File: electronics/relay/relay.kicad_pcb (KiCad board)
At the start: 2 copper layers, 17 x 49 mm, 16 parts, among them J1 Conn_01x01_Female, J2 Conn_01x01_Female, J3 Conn_01x01_Female, J4 Conn_01x01_Female, J5 Conn_01x01_Female, J6 Conn_01x01_Female, J7 Conn_01x01_Female, J8 Conn_01x01_Female, J9 Conn_01x01_Female, K1 SANYOU_SRD_Form_C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

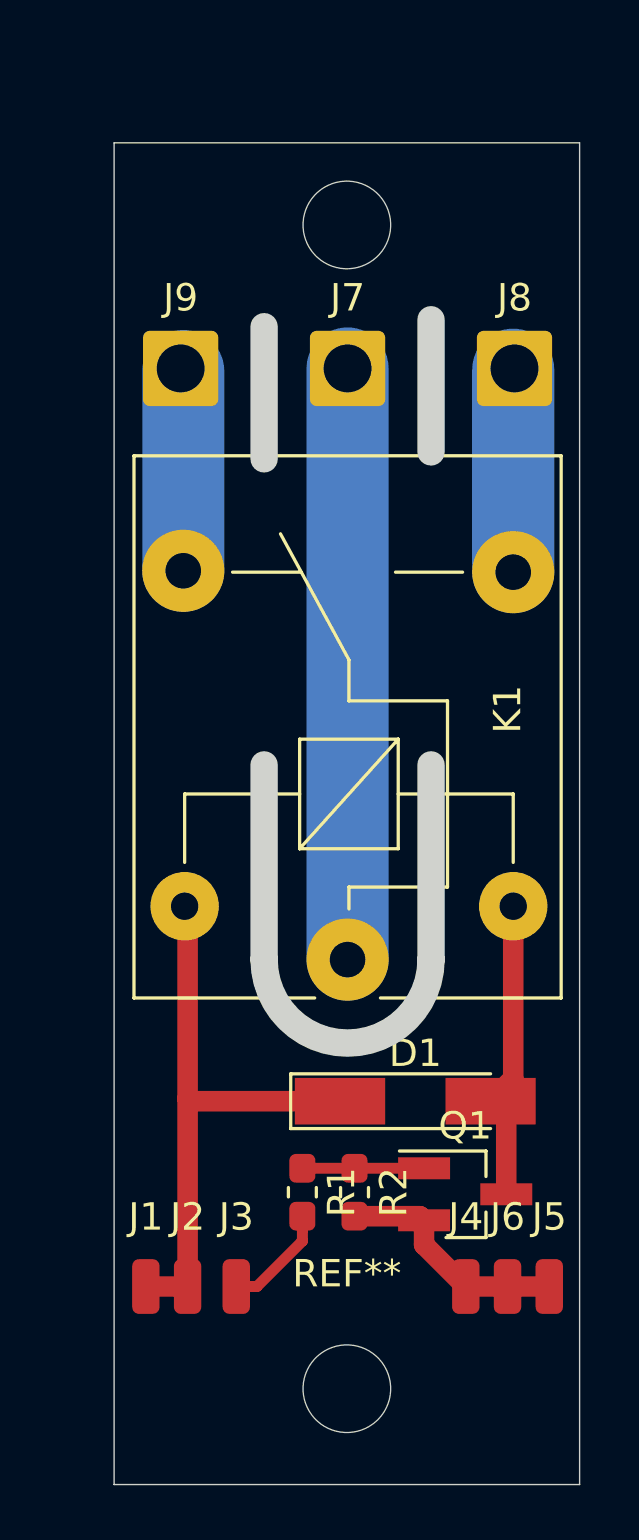
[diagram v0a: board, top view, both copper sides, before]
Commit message: Relay board ready, ESP3266 redesign (GPIO16 instead of GPIO0)
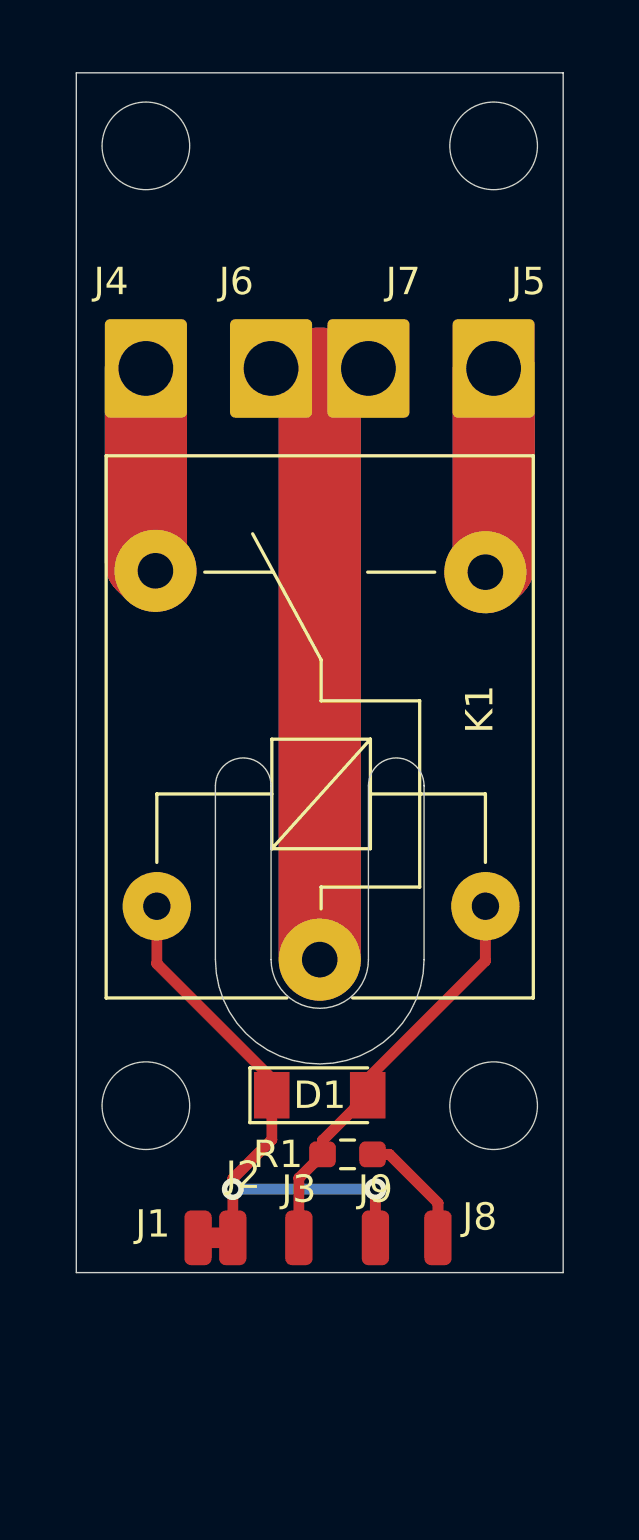
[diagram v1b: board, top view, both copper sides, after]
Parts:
- removed Q1: Q_NMOS_GSD, Package_TO_SOT_SMD:SOT-23_Handsoldering
- removed R2: R_Small, Resistor_SMD:R_0603_1608Metric_Pad1.05x0.95mm_HandSolder
- removed the REF** at (144.5, 116.0)
- removed the REF** at (144.5, 73.5)
- added REF**: MountingHole_3.2mm_M3, MountingHole:MountingHole_3.2mm_M3, F.Cu at (149.9, 70.6)
- added REF**: MountingHole_3.2mm_M3, MountingHole:MountingHole_3.2mm_M3, F.Cu at (149.9, 105.7)
- added REF**: MountingHole_3.2mm_M3, MountingHole:MountingHole_3.2mm_M3, F.Cu at (137.2, 70.6)
- added REF**: MountingHole_3.2mm_M3, MountingHole:MountingHole_3.2mm_M3, F.Cu at (137.2, 105.7)
- D1: footprint Diode_SMD:D_MiniMELF_Handsoldering -> Diode_SMD:D_MiniMELF
- J4, J5, J6: footprint Connector_Wire:SolderWirePad_1x01_SMD_1x2mm -> Powerstrip:SolderWire-Mains
- J7: footprint Connector_Wire:SolderWire-1sqmm_1x01_D1.4mm_OD2.7mm -> Powerstrip:SolderWire-Mains
- J8, J9: footprint Connector_Wire:SolderWire-1sqmm_1x01_D1.4mm_OD2.7mm -> Connector_Wire:SolderWirePad_1x01_SMD_1x2mm
- R1: value R_Small -> 470R; footprint Resistor_SMD:R_0603_1608Metric_Pad1.05x0.95mm_HandSolder -> Resistor_SMD:R_0603_1608Metric_Pad0.98x0.95mm_HandSolder
- moved J4 35.5 mm to (137.2, 78.7), turned to 180 degrees
- moved J6 34.6 mm to (141.7, 78.7), turned to 180 degrees
- moved J5 33.6 mm to (149.9, 78.7), turned to 180 degrees
- moved J9 32.5 mm to (145.5, 110.5)
- moved J8 31.9 mm to (147.8, 110.5)
- moved D1 3.50 mm to (143.5, 105.3)
- moved J3 2.90 mm to (142.7, 110.5)
- moved J1 2.61 mm to (139.1, 110.5)
- moved J2 2.43 mm to (140.3, 110.5)
- moved R1 2.15 mm to (144.5, 107.4), turned to 180 degrees
- moved K1 1.02 mm to (143.5, 100.3)
- moved J7 0.76 mm to (145.3, 78.7), turned to 180 degrees
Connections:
- J3 pad 1: Net-(J3-Pad1) -> Net-(D1-Pad2)
- J4 pad 1: GND -> Net-(J4-Pad1)
- J5 pad 1: GND -> Net-(J5-Pad1)
- J6 pad 1: GND -> Net-(J6-Pad1)
- J7 pad 1: Net-(J7-Pad1) -> Net-(J6-Pad1)
- J9 pad 1: Net-(J9-Pad1) -> Net-(D1-Pad1)
- K1 pad 1: Net-(J7-Pad1) -> Net-(J6-Pad1)
- K1 pad 3: Net-(J8-Pad1) -> Net-(J5-Pad1)
- K1 pad 4: Net-(J9-Pad1) -> Net-(J4-Pad1)
- R1 pad 1: Net-(Q1-Pad1) -> Net-(J8-Pad1)
- R1 pad 2: Net-(J3-Pad1) -> Net-(D1-Pad2)
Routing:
- net Net-(J6-Pad1): track 0.00 -> 46.7 mm
- net Net-(J7-Pad1): track 21.6 -> 0.00 mm
- net Net-(J5-Pad1): track 0.00 -> 15.1 mm
- net Net-(J4-Pad1): track 0.00 -> 15.1 mm
- net GND: track 8.70 -> 0.00 mm
- net Net-(J9-Pad1): track 7.43 -> 0.00 mm
- net Net-(Q1-Pad1): track 4.44 -> 0.00 mm
- net Net-(J3-Pad1): track 4.01 -> 0.00 mm
- net Net-(D1-Pad2): track 11.1 -> 15.0 mm
- net Net-(J8-Pad1): track 7.46 -> 4.40 mm
- net Net-(D1-Pad1): track 21.1 -> 22.7 mm, vias 0 -> 2
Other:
- board size 17 x 49 mm -> 17.8 x 43.8 mm
- net class Current removed
- net class Mains removed

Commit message: Small PCB modifications, esphome config added
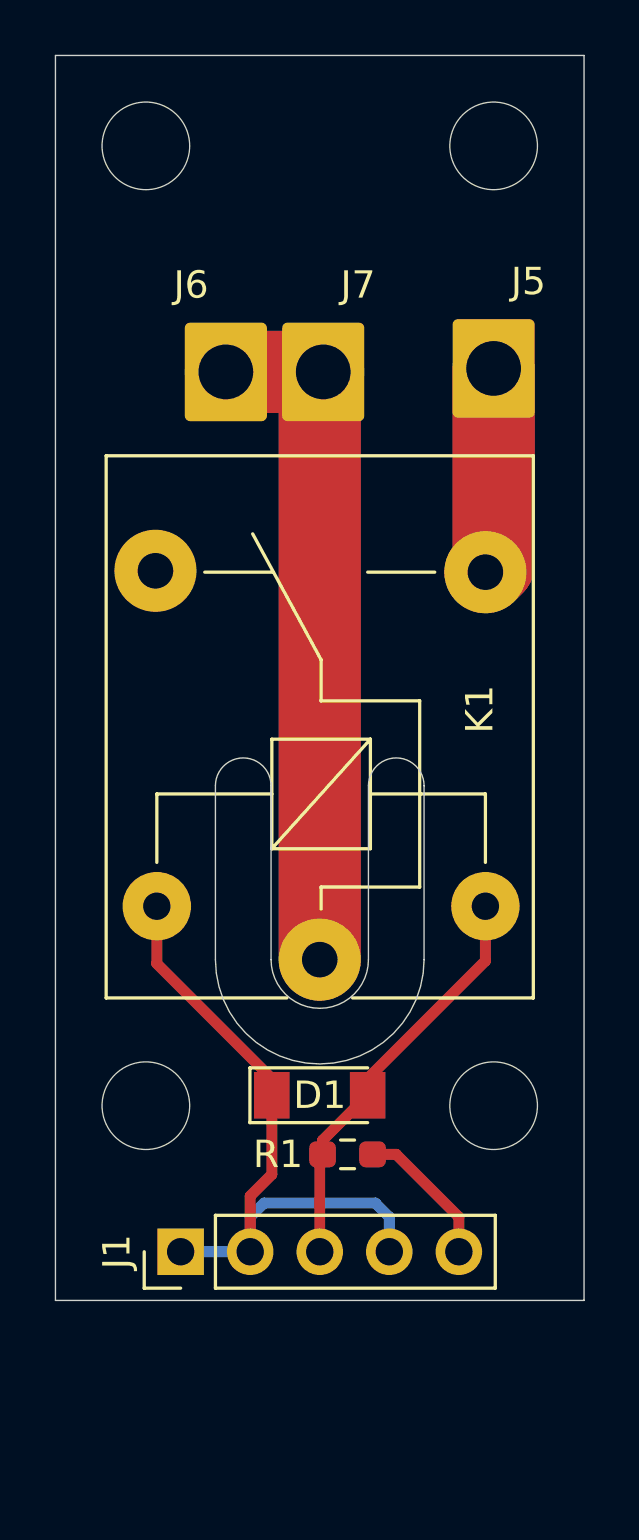
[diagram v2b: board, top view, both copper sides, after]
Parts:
- removed J2, J3, J8, J9: Conn_01x01_Female, Connector_Wire:SolderWirePad_1x01_SMD_1x2mm
- removed J4: Conn_01x01_Female, Powerstrip:SolderWire-Mains
- J1: value Conn_01x01_Female -> Conn_01x05; footprint Connector_Wire:SolderWirePad_1x01_SMD_1x2mm -> Connector_PinHeader_2.54mm:PinHeader_1x05_P2.54mm_Vertical
- moved J6 1.66 mm to (140.1, 78.9)
- moved J7 1.66 mm to (143.6, 78.9)
- moved J1 0.81 mm to (138.4, 111.0), turned to 90 degrees
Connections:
- K1 pad 4: Net-(J4-Pad1) -> (no net)
- R1 pad 1: Net-(J8-Pad1) -> Net-(J1-Pad5)
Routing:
- net Net-(J4-Pad1): track 15.1 -> 0.00 mm
- net Net-(J1-Pad5): track 0.00 -> 5.37 mm
- net Net-(J8-Pad1): track 4.40 -> 0.00 mm
- net Net-(J6-Pad1): track 46.7 -> 50.3 mm
- net Net-(D1-Pad1): track 22.7 -> 25.3 mm, vias 2 -> 0
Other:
- board size 17.8 x 43.8 mm -> 19.3 x 45.5 mm

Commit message: PCB 1st batch
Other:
- rule pad_to_mask_clearance: 0.051 -> 0
